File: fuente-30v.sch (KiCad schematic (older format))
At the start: 30 parts, among them P1 POT, P2 POT, Q1-CONN1 CONN_01X03, Q2 BD137, Q3 BD139, Q4 BC167, Q5 BC167, T1 TRANSFO, con3 CONN_01X02

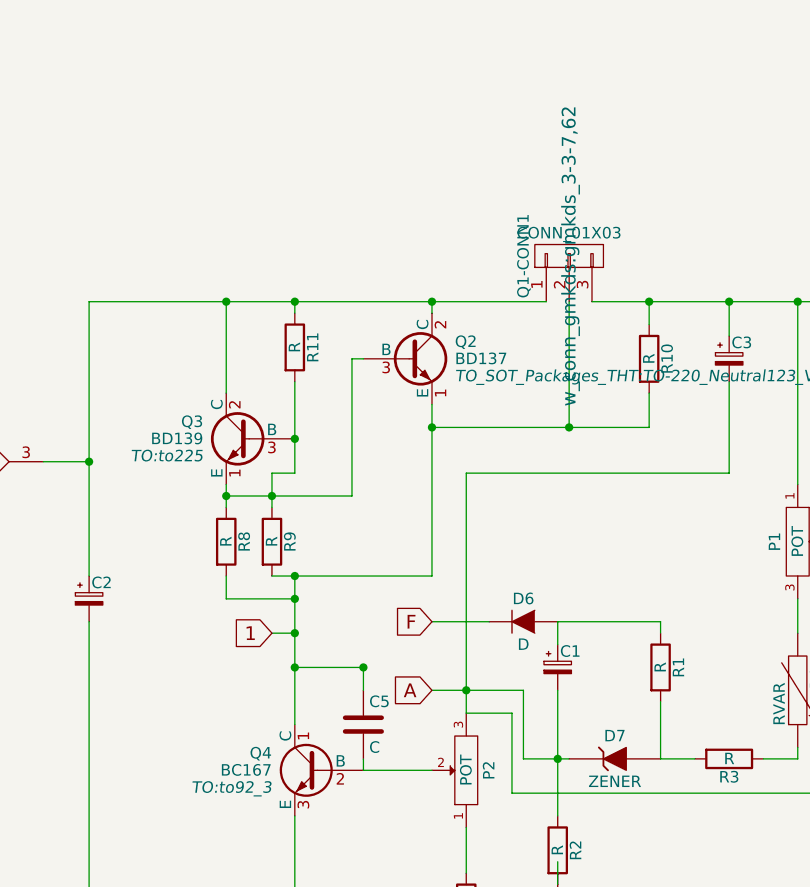
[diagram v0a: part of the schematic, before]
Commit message: version 1.1: arreglados los problemas de conexion
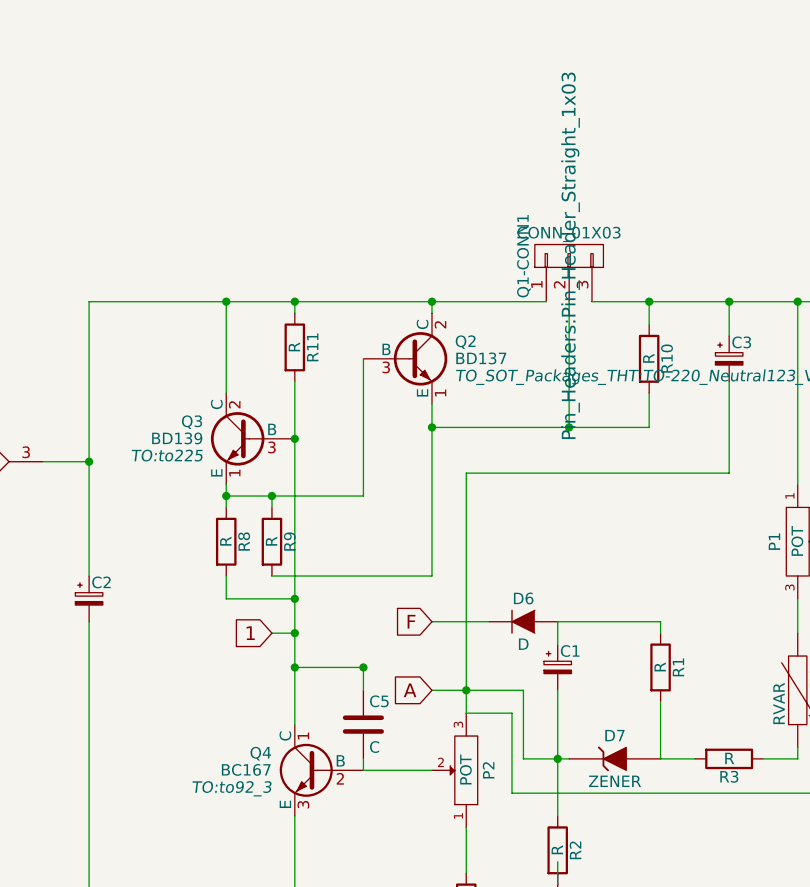
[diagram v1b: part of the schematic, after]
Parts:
- Q1-CONN1: footprint w_conn_gmkds:gmkds_3-3-7,62 -> Pin_Headers:Pin_Header_Straight_1x03
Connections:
- net 1: now also Q3.3 (B), R11.2; no longer Q1-CONN1.2 (P2), Q2.1 (E), R10.2, R9.2
- net at Q2.3 (B), Q3.1 (E), R8.1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: no longer Q3.3 (B), R11.2
- new net: Q1-CONN1.2 (P2), Q2.1 (E), R10.2, R9.2
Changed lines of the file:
@@
 	5700 3100 5700 3200
 Wire Wire Line
-	5900 3050 5900 3200
-Wire Wire Line
-	5700 3150 6250 3150
+	5900 3150 5900 3200
+Wire Wire Line
+	5700 3150 6300 3150
 Connection ~ 5700 3150
 Wire Wire Line
 	6000 2300 6000 2350
 Connection ~ 5700 2300
-Wire Wire Line
-	6250 3150 6250 2550
-Wire Wire Line
-	6250 2550 6300 2550
 Connection ~ 5900 3150
 Wire Wire Line
@@
 Connection ~ 9350 4450
 Wire Wire Line
-	5700 3600 6000 3600
+	6000 3600 5700 3600
 Wire Wire Line
 	6000 3900 6300 3900
@@
 	2750 5150 3000 5150
 Wire Wire Line
-	6000 2650 6000 3050
-Wire Wire Line
-	6000 3050 5900 3050
-Connection ~ 6000 3500
-Wire Wire Line
-	5700 3500 5700 3600
+	6000 2650 6000 4150
+Wire Wire Line
+	5700 3600 5700 3500
 Wire Wire Line
 	6300 3900 6300 4000
-Wire Wire Line
-	6000 3500 6000 4150
 Wire Wire Line
 	6950 4450 9800 4450
@@
 F 0 "Q1-CONN1" H 7200 2300 50  0000 C CNN
 F 1 "CONN_01X03" V 7300 2100 50  0000 C CNN
-F 2 "w_conn_gmkds:gmkds_3-3-7,62" H 7200 2100 60  0000 C CNN
+F 2 "Pin_Headers:Pin_Header_Straight_1x03" H 7200 2100 60  0000 C CNN
 F 3 "" H 7200 2100 60  0000 C CNN
 	1    7200 2100
@@
 	7200 2300 7200 2850
 Connection ~ 7200 2850
+Wire Wire Line
+	6300 3150 6300 2550
 $EndSCHEMATC

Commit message: change track width to 1 mm
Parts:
- C2: footprint Capacitors_Elko_ThroughHole:Elko_vert_31.5x16mm_RM7.5 -> w_capacitors:CP_22x25mm
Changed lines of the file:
@@
 LIBS:contrib
 LIBS:valves
-LIBS:transfo
 LIBS:fuente-30v-cache
 EELAYER 25 0
@@
 F 0 "C2" H 5110 3670 50  0000 L CNN
 F 1 " " H 5110 3520 50  0000 L CNN
-F 2 "Capacitors_Elko_ThroughHole:Elko_vert_31.5x16mm_RM7.5" H 5100 3600 60  0001 C CNN
+F 2 "w_capacitors:CP_22x25mm" H 5100 3600 60  0001 C CNN
 F 3 "" H 5100 3600 60  0000 C CNN
 	1    5100 3600

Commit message: checked and fixed design rules
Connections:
- net at D2.2, con3.1 (P1): now also T1.5 (AB)
- net at D2.4, con3.2 (P2): now also T1.1 (AA)
- no-connect marks 2 -> 0
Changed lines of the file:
@@
 Text GLabel 3000 5150 2    60   Input ~ 0
 A
-NoConn ~ 1950 4750
-NoConn ~ 1950 5150
 Wire Wire Line
 	4900 3000 5100 3000
@@
 	2750 2900 2750 2750
 Wire Wire Line
-	2750 3000 2750 3150
+	2750 3000 2750 3600
 $Comp
 L CONN_01X03 Q1-CONN1
@@
 Wire Wire Line
 	6300 3150 6300 2550
+Wire Wire Line
+	1950 4750 1950 3450
+Wire Wire Line
+	1950 3450 2950 3450
+Wire Wire Line
+	2950 3450 2950 2750
+Connection ~ 2950 2750
+Wire Wire Line
+	1950 5150 1800 5150
+Wire Wire Line
+	1800 5150 1800 3600
+Wire Wire Line
+	1800 3600 2750 3600
+Connection ~ 2750 3150
 $EndSCHEMATC
